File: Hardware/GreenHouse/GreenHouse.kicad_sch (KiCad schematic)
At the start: 25 parts, among them J1 12 V IN, J2 SENSORES TEMP, J3 DRIVER NEMA DERECHO, J4 DRIVER NEMA IZQUIERDO, J5 SEÑAL DESCANSO MOTOR, J6 FIN CARRERA, J7 FIN CARRERA VCC 5V, J8 SEÑAL MOTORES, U1 Ard_Pro_mini

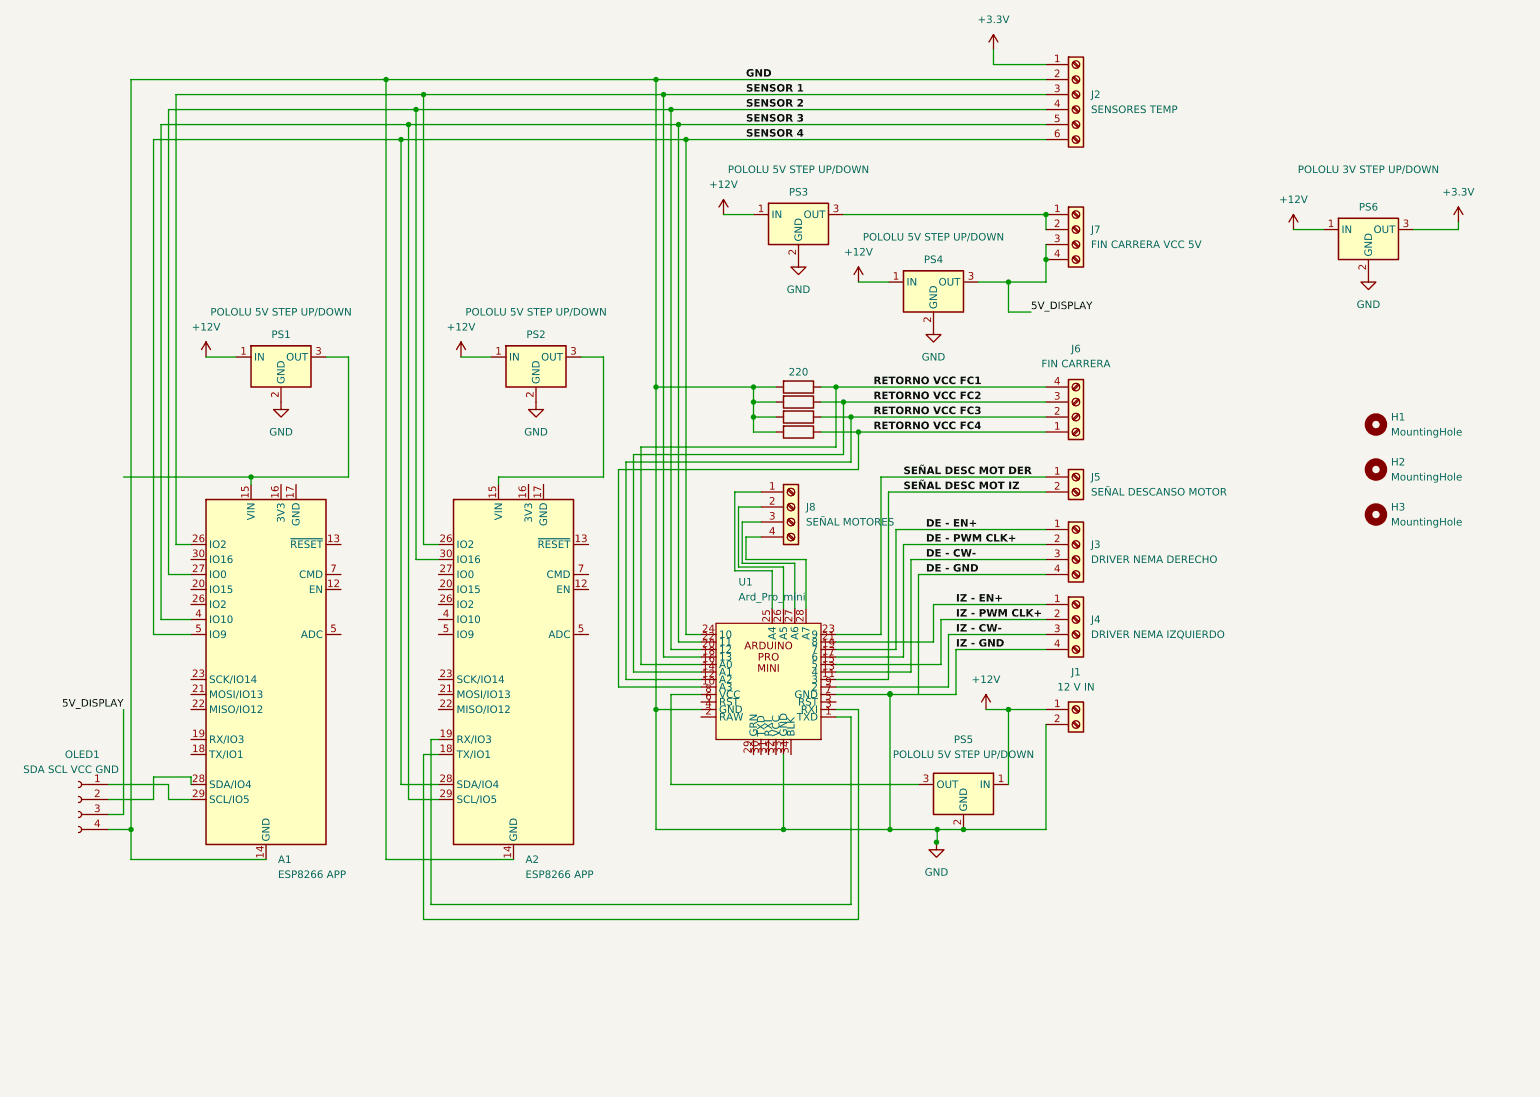
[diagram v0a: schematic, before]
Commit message: fix: reduce the board size & re trace some parts.
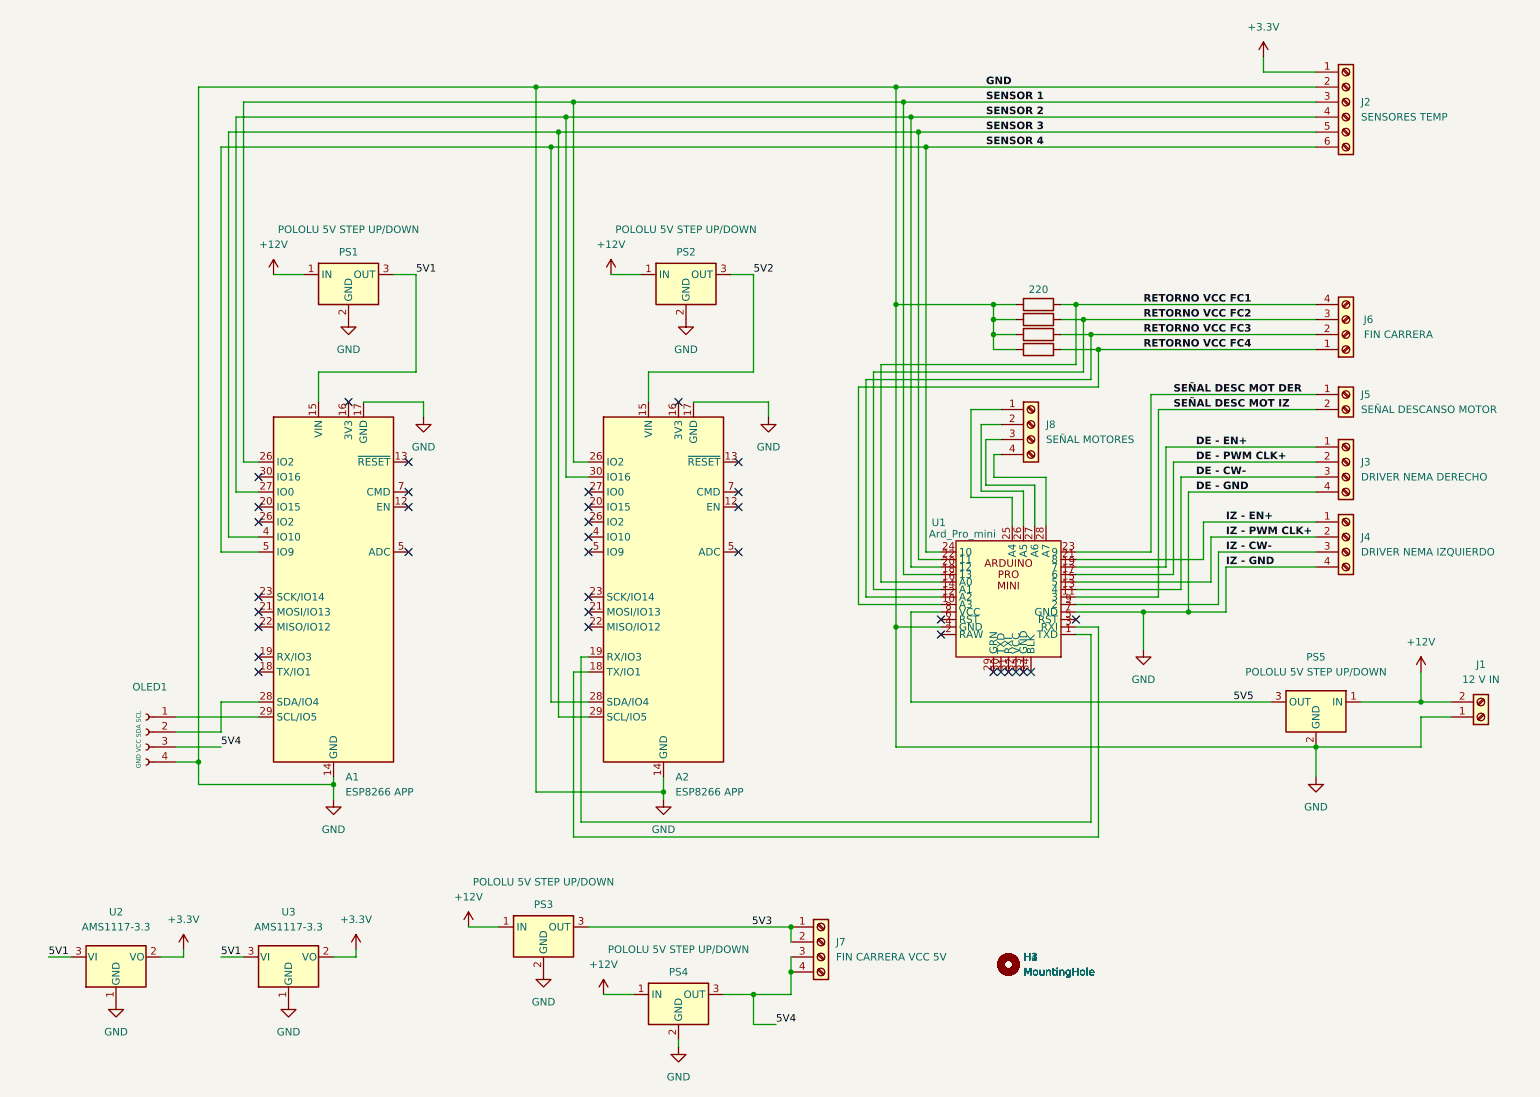
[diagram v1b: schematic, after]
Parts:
- removed PS6: POLOLU 3V STEP UP/DOWN, Converter_DCDC:Converter_DCDC_Murata_OKI-78SR_Horizontal, symbol Converter_DCDC:OKI-78SR-5_1.5-W36H-C
- added H4: MountingHole, MountingHole:MountingHole_3.2mm_M3, symbol Mechanical:MountingHole
- added U2, U3: AMS1117-3.3, Package_TO_SOT_SMD:SOT-223-3_TabPin2, symbol Regulator_Linear:AMS1117-3.3
- OLED1: value SDA SCL VCC GND -> GND VCC SDA SCL; footprint Connector_Molex:Molex_KK-396_A-41791-0004_1x04_P3.96mm_Vertical -> Connector_PinHeader_2.54mm:PinHeader_1x04_P2.54mm_Vertical
- R1, R2, R3, R4: footprint Resistor_THT:R_Axial_DIN0411_L9.9mm_D3.6mm_P15.24mm_Horizontal -> Resistor_THT:R_Axial_DIN0309_L9.0mm_D3.2mm_P12.70mm_Horizontal
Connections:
- net DE - GND is gone; now on net GND: J3.4 (Pin_4)
- net +12V: now also J1.2 (Pin_2); no longer J1.1 (Pin_1)
- net +3.3V: now also U2.2 (VO), U3.2 (VO)
- net GND: now also A1.17 (GND), A2.17 (GND), J1.1 (Pin_1), U2.1 (GND), U3.1 (GND); no longer J1.2 (Pin_2), U1.33 (GND)
- net 5V3: now reaches J7.1 (Pin_1), J7.2 (Pin_2), PS3.3 (OUT)
- net 5V1: now reaches A1.15 (VIN), PS1.3 (OUT)
- net 5V1: now also U2.3 (VI), U3.3 (VI)
- net 5V5: now reaches PS5.3 (OUT), U1.8 (VCC)
- net 5V2: now reaches A2.15 (VIN), PS2.3 (OUT)
- net 5V_DISPLAY renamed 5V4
- no-connect marks 0 -> 35
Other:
- moved on the sheet: A1, A2, H1, H2, H3, J1, J2, J3, J4, J5, J6, J7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

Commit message: docs: add Boom in Html
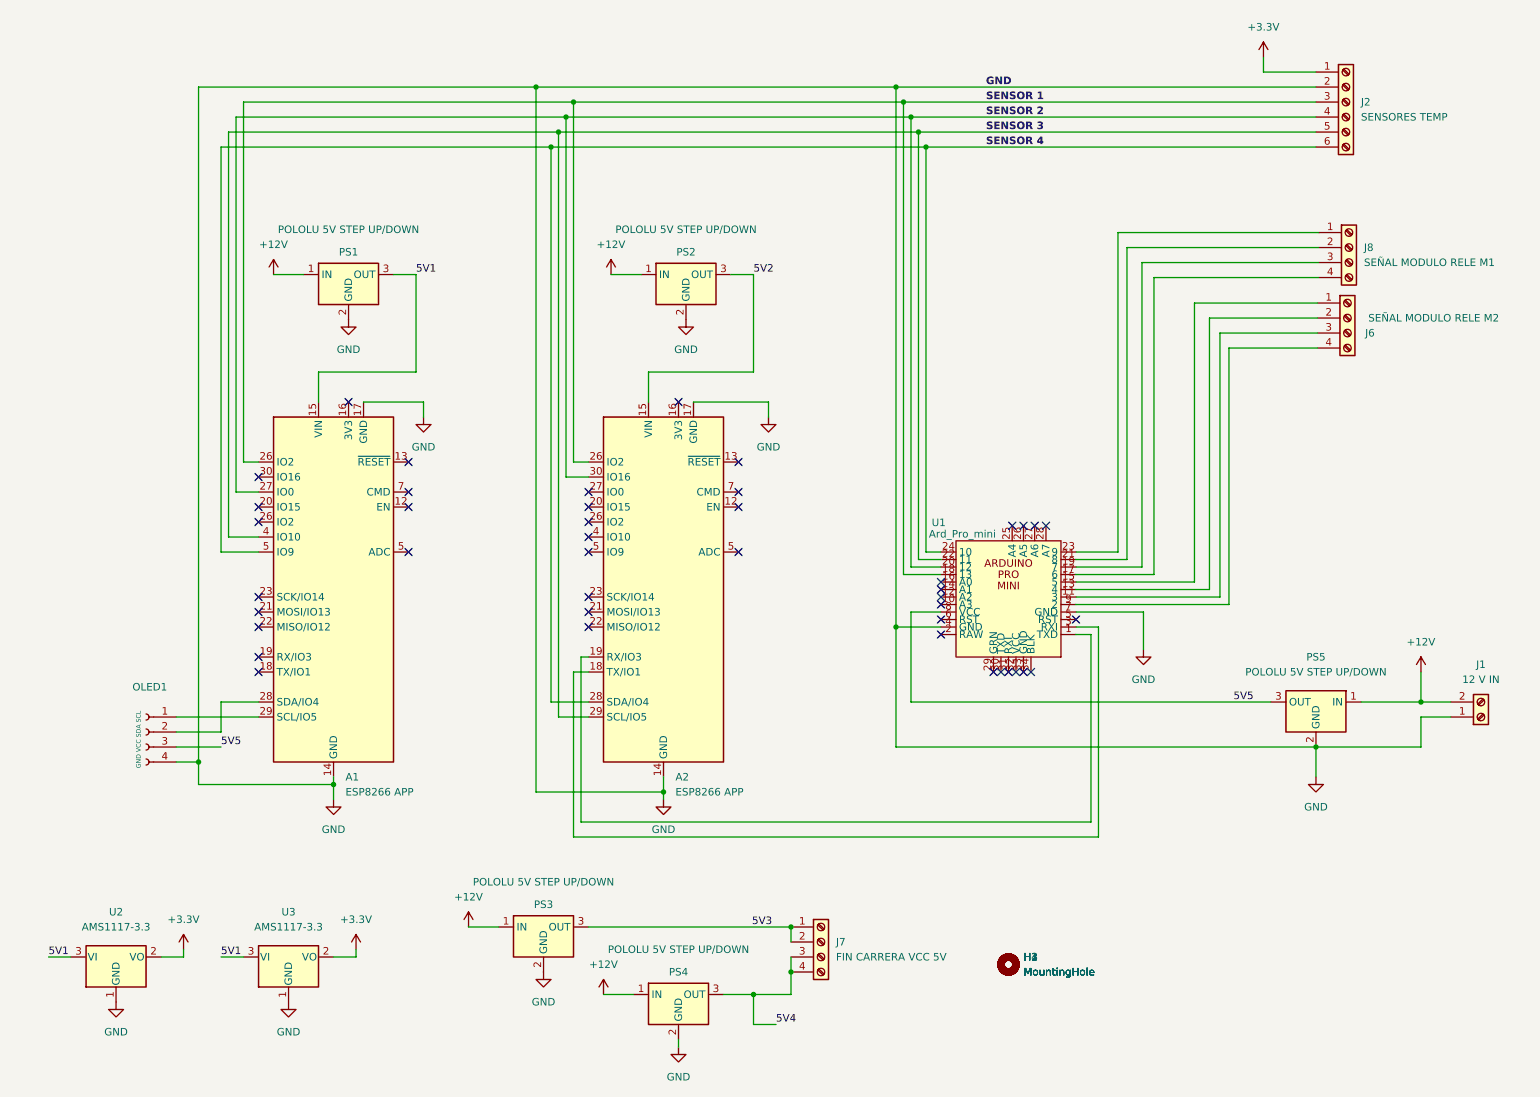
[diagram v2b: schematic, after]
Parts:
- removed J3: DRIVER NEMA DERECHO, TerminalBlock:TerminalBlock_bornier-4_P5.08mm, symbol Connector:Screw_Terminal_01x04
- removed J4: DRIVER NEMA IZQUIERDO, TerminalBlock:TerminalBlock_bornier-4_P5.08mm, symbol Connector:Screw_Terminal_01x04
- removed J5: SEÑAL DESCANSO MOTOR, TerminalBlock:TerminalBlock_bornier-2_P5.08mm, symbol Connector:Screw_Terminal_01x02
- removed R1, R2, R3, R4: 220, Resistor_THT:R_Axial_DIN0309_L9.0mm_D3.2mm_P12.70mm_Horizontal, symbol Device:R
- J6: value FIN CARRERA -> SEÑAL MODULO RELE M2
- J8: value SEÑAL MOTORES -> SEÑAL MODULO RELE M1
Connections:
- net DE - EN+ is gone; now on an unnamed net: U1.19 (7)
- net DE - PWM CLK+ is gone; now on an unnamed net: U1.17 (6)
- net IZ - EN+ is gone; now on an unnamed net: U1.21 (8)
- net SEÑAL DESC MOT DER is gone; now on an unnamed net: U1.23 (9)
- net SEÑAL DESC MOT IZ is gone; now on an unnamed net: U1.11 (3)
- net 5V4: no longer OLED1.3 (Pin_3)
- net 5V5: now also OLED1.3 (Pin_3)
- net at J8.1 (Pin_1): no longer U1.25 (A4)
- net at J8.2 (Pin_2): no longer U1.26 (A5)
- net at J8.3 (Pin_3): no longer U1.27 (A6)
- net at J8.4 (Pin_4): no longer U1.28 (A7)
- net DE - CW-: no longer names the net of U1.13 (4)
- net DE - CW-: now also J6.2 (Pin_2)
- net IZ - CW-: no longer names the net of U1.9 (2)
- net IZ - CW-: now also J6.4 (Pin_4)
- net IZ - PWM CLK+: no longer names the net of U1.15 (5)
- net IZ - PWM CLK+: now also J6.1 (Pin_1)
- net RETORNO VCC FC1: no longer names the net of U1.16 (A0)
- net RETORNO VCC FC1: no longer J6.4 (Pin_4)
- net RETORNO VCC FC2: no longer names the net of J6.3 (Pin_3)
- net RETORNO VCC FC2: no longer U1.14 (A1)
- net RETORNO VCC FC3: no longer names the net of U1.12 (A2)
- net RETORNO VCC FC3: no longer J6.2 (Pin_2)
- net RETORNO VCC FC4: no longer names the net of U1.10 (A3)
- net RETORNO VCC FC4: no longer J6.1 (Pin_1)
- no-connect marks 35 -> 43
